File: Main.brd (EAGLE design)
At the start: 100 x 130 mm, 78 parts, among them M1 MOSFET

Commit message: power block layout
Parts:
- R2, R4: device SamuelLibrary:RESC6232X120N -> SamuelLibrary:RESC1508X45N
- R3: device SamuelLibrary:RESC5025X70N -> SamuelLibrary:RESC1508X45N
- moved R4 109.8 mm to (10.0, 120.7), turned to 180 degrees
- moved R3 106.0 mm to (10.9, 123.0), turned to 90 degrees
- moved C4 84.2 mm to (10.0, 118.7)
- moved I2C 81.1 mm to (3.96, 77.1)
- moved CAN 76.2 mm to (15.2, 88.6), turned to 270 degrees
- moved R6 68.6 mm to (17.8, 87.2), turned to 90 degrees
- moved SN65 58.7 mm to (23.0, 87.2), turned to 180 degrees
- moved MCP2515 49.2 mm to (34.3, 85.7)
- moved C8 45.1 mm to (1.11, 95.7)
- moved C7 38.2 mm to (1.07, 98.4)
- moved C6 31.3 mm to (1.06, 101.2)
- moved R1 25.2 mm to (-20.4, 123.9)
- moved C9 23.9 mm to (8.85, 123.0), turned to 270 degrees
- moved R2 13.7 mm to (7.62, 113.9), turned to 90 degrees
- moved C3 8.90 mm to (12.6, 115.6), turned to 270 degrees
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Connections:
- net GND: now also MP2238.10, MP2238.6; no longer MP2238.AGND, MP2238.GND
- net N$2: now also MP2238.12; no longer MP2238.VCC
- net N$3: now also MP2238.3; no longer MP2238.BST
- net N$4: now also MP2238.1; no longer MP2238.EN
- net N$45: now also MP2238.11; no longer MP2238.FB
- net N$49: now also MP2238.2; no longer MP2238.SW
- net VBATT+: now also MP2238.9; no longer MP2238.IN
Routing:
- net N$34: track 14.0 -> 11.0 mm
- net N$35: track 13.7 -> 11.8 mm
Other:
- outline, holes or cut-outs redrawn

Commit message: dope pwr led system
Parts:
- removed PWR: (no value), SamuelLibrary:WL-SMCC_0603_R_Y_V
- added D1, D10, D2, D3, D4, D5, D6, D7, D8, D9: (no value), SamuelLibrary:WL-SMCD_0603
- added M2: MOSFET, SamuelLibrary:SOT95P240X100-3N
- added R33, R34, R35, R36: 49.9, SamuelLibrary:RESC1508X45N
- added R37: 10k, SamuelLibrary:RESC3116X55N
- added R38: 120, SamuelLibrary:RESC1508X45N
- R1: value 300k -> (none); device SamuelLibrary:RESC6232X120N -> SamuelLibrary:RESC1508X45N
- R32: value 165 -> 49.9; device SamuelLibrary:RESC2012X45N -> SamuelLibrary:RESC1508X45N
- moved R32 223.9 mm to (-93.0, -14.0), turned to 0 degrees
- moved C12 133.1 mm to (44.4, 20.2)
- moved C13 133.1 mm to (31.7, 20.2)
- moved C14 133.1 mm to (38.0, 20.2)
- moved C15 131.4 mm to (52.7, 25.2)
- moved R1 26.4 mm to (5.00, 117.0), turned to 180 degrees
- moved GPIO 25.0 mm to (74.5, 77.5)
- moved R31 14.9 mm to (97.0, 104.5), turned to 180 degrees
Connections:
- removed net 6V: PWM0.2, PWM1.2
- removed net N$42: GPIO.18
- removed net N$54: PWR.2, R31.2
- new net N$18: D7.2, R35.2
- new net N$19: D10.2, D9.1
- new net N$23: M2.3, R37.2, R38.1
- new net N$24: D10.1, D2.1, D4.1, D6.1, D8.1, M2.1
- new net N$5: D1.1, D2.2
- new net N$7: D1.2, R32.2
- net +5V: now also PWM0.2, PWM1.2, R32.1, R33.1, R34.1, R35.1, R36.1
- net COMM_GRN: now also GPIO.18; no longer GPIO.22
- net DIO0: now also GPIO.21
- net DIO1: now also GPIO.22
- net DIO2: now also GPIO.23
- net DIO3: now also GPIO.32
- net DIO4: now also GPIO.33
- net DIO5: now also GPIO.35
- net DIO6: now also GPIO.36
- net DIO7: now also GPIO.37
- net GND: now also M2.2, R31.1, R37.1; no longer PWR.1, R32.1
- net N$10: now also D5.1, D6.2; no longer GPIO.35
- net N$12: now also D5.2, R34.2; no longer GPIO.33
- net N$13: now also D7.1, D8.2; no longer GPIO.32
- net N$22: now also D9.2, R36.2; no longer GPIO.23
- net N$56: now also R31.2; no longer R32.2
- net N$8: now also D3.1, D4.2; no longer GPIO.37
- net N$9: now also D3.2, R33.2; no longer GPIO.36
- net PWR: now also R38.2; no longer GPIO.21, R31.1
- net SPI_MISO: now also GPIO.11; no longer GPIO.10
- net SPI_MOSI: now also GPIO.10; no longer GPIO.11

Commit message: dope led system led placement
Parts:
- removed ADC124S051: ADC124S051, SamuelLibrary:SOP50P490X110-10N
- removed LP2590: LP2950ACDT−5.0, SamuelLibrary:TO229P990X238-3N
- added ADC124: ADC124S051, SamuelLibrary:SOP50P490X110-10N
- added LP2950: LP2950ACDT−5.0, SamuelLibrary:TO229P990X238-3N
- moved D10 219.6 mm to (82.0, 72.0), turned to 90 degrees
- moved D9 209.2 mm to (81.0, 58.0), turned to 90 degrees
- moved D8 197.2 mm to (80.0, 44.0), turned to 90 degrees
- moved D7 189.1 mm to (79.0, 30.0), turned to 90 degrees
- moved M2 187.2 mm to (55.0, 47.0)
- moved R37 187.2 mm to (53.0, 39.0)
- moved R38 187.2 mm to (53.0, 32.0)
- moved D6 173.6 mm to (70.0, 18.0), turned to 270 degrees
- moved R34 161.2 mm to (42.0, 55.0)
- moved R35 160.2 mm to (42.0, 42.0)
- moved R36 159.2 mm to (42.0, 29.0)
- moved R32 152.0 mm to (28.0, 78.0)
- moved R33 144.5 mm to (34.0, 46.0)
- moved D1 137.3 mm to (18.0, 72.0), turned to 90 degrees
- moved D5 135.0 mm to (30.0, 18.0), turned to 270 degrees
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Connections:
- removed net N$28: GPIO.4
- removed net N$29: GPIO.5
- removed net N$30: GPIO.6
- removed net N$31: GPIO.7
- removed net N$32: GPIO.8
- removed net N$39: GPIO.15
- net +5V: now also LP2950.1, R32.2, R33.2, R34.2, R35.2, R36.2; no longer LP2590.1, R32.1, R33.1, R34.1, R35.1, R36.1
- net AI0: now also ADC124.9; no longer ADC124S051.9
- net AI1: now also ADC124.10; no longer ADC124S051.10
- net AI2: now also ADC124.5; no longer ADC124S051.5
- net AI3: now also ADC124.4; no longer ADC124S051.4
- net AN_CS: now also ADC124.1, GPIO.4; no longer ADC124S051.1
- net AN_DIN: now also ADC124.8, GPIO.7; no longer ADC124S051.8
- net AN_DOUT: now also ADC124.7, GPIO.6; no longer ADC124S051.7
- net AN_SCLK: now also ADC124.6, GPIO.5; no longer ADC124S051.6
- net GND: now also ADC124.3, LP2950.3; no longer ADC124S051.3, LP2590.2
- net N$12: now also R34.1; no longer R34.2
- net N$18: now also R35.1; no longer R35.2
- net N$22: now also R36.1; no longer R36.2
- net N$38: now also ADC124.2, LP2950.2; no longer ADC124S051.2, LP2590.3
- net N$7: now also R32.1; no longer R32.2
- net N$9: now also R33.1; no longer R33.2
- net PWR: now also GPIO.15
- net RSL: now also GPIO.8
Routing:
- net N$35: track 11.8 -> 3.37 mm
- net N$34: track 11.0 -> 2.70 mm
- net N$56: track 5.66 -> 1.00 mm
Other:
- outline, holes or cut-outs redrawn

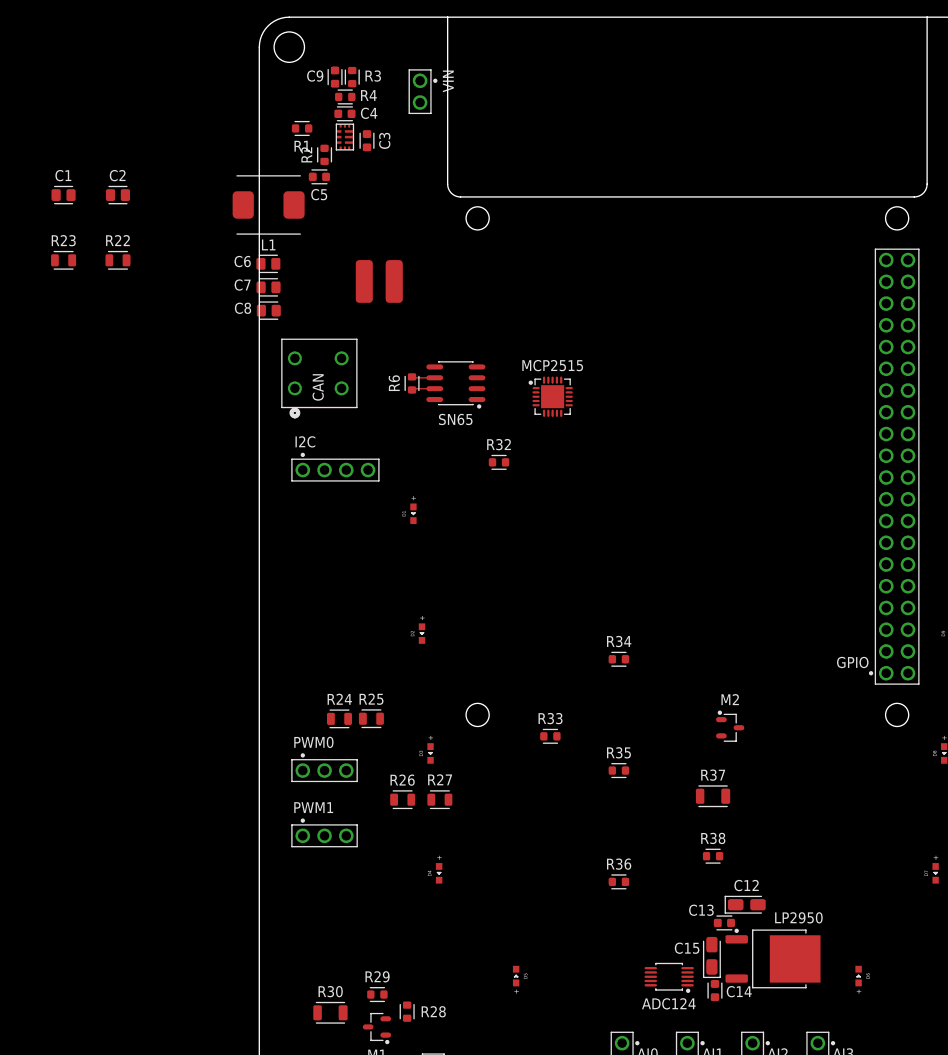
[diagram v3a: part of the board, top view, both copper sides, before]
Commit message: board layout and planes
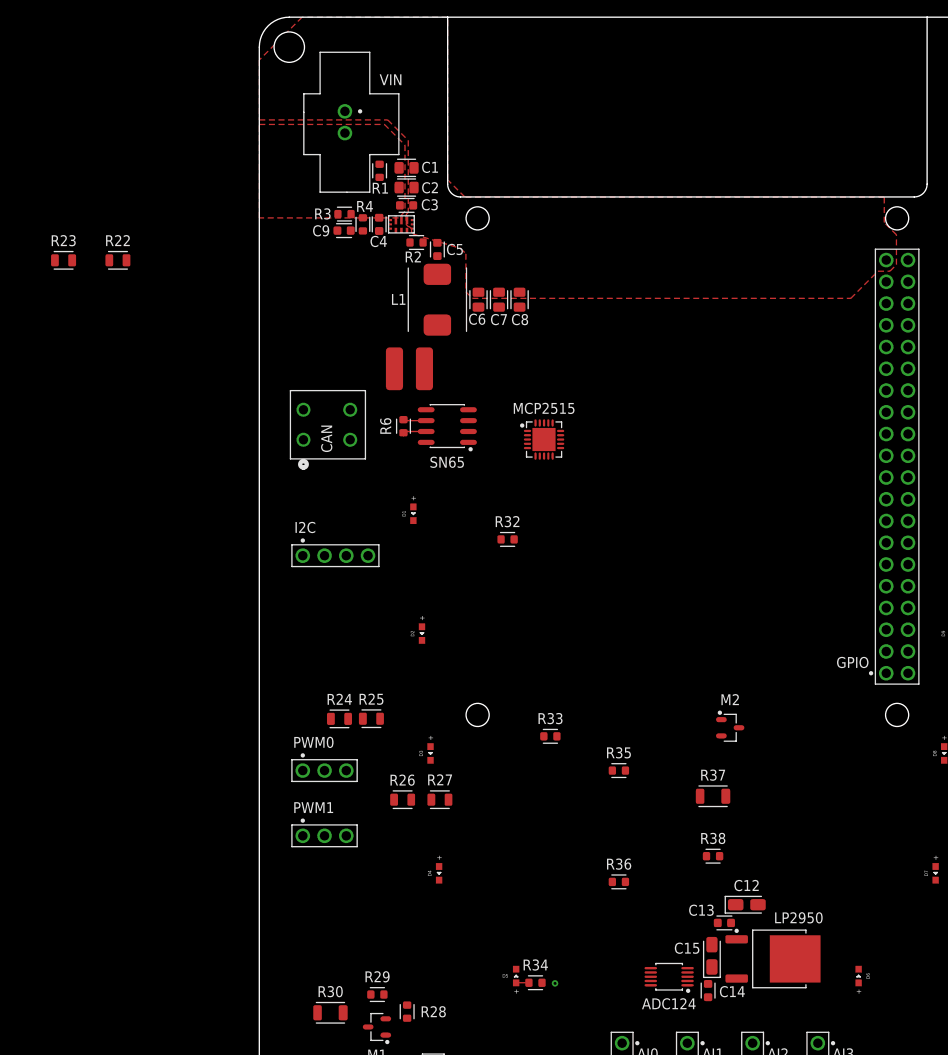
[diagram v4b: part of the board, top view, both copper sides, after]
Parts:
- VIN: value 2X1_MALE_HEADER_PIN -> CTF020V8; device SamuelLibrary:HDRV2W64P254_1X2_508X254X838B -> SamuelLibrary:CTF020V8
- moved C1 40.2 mm to (17.2, 112.4)
- moved R34 39.0 mm to (32.3, 17.2)
- moved C2 33.7 mm to (17.2, 110.1)
- moved C8 29.3 mm to (30.4, 97.0), turned to 90 degrees
- moved C7 27.0 mm to (28.0, 97.0), turned to 90 degrees
- moved C6 24.9 mm to (25.6, 97.0), turned to 90 degrees
- moved L1 22.6 mm to (20.8, 97.0), turned to 270 degrees
- moved C9 18.0 mm to (9.90, 105.1), turned to 0 degrees
- moved C5 16.2 mm to (20.8, 102.9), turned to 270 degrees
- moved R3 16.0 mm to (9.95, 107.0), turned to 180 degrees
- moved R4 15.0 mm to (12.1, 105.8), turned to 270 degrees
- moved R2 14.8 mm to (18.4, 103.7), turned to 180 degrees
- moved C4 13.5 mm to (14.0, 105.8), turned to 90 degrees
- moved MP2238 12.1 mm to (16.6, 105.8), turned to 90 degrees
- moved USB_PWR 10.8 mm to (17.5, 88.9), turned to 180 degrees
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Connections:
- net GND: now also VIN.1; no longer VIN.2
- net VBATT+: now also VIN.2; no longer VIN.1
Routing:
- net N$12: track 0.00 -> 1.50 mm
- added copper zone on layer 2, net 5V
- added copper zone on layer 1, net GND
- added copper zone on layer 15, net GND
- added copper zone on layer 1, net VBATT+
